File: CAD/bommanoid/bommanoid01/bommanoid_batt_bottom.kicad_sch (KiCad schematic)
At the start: 6 parts

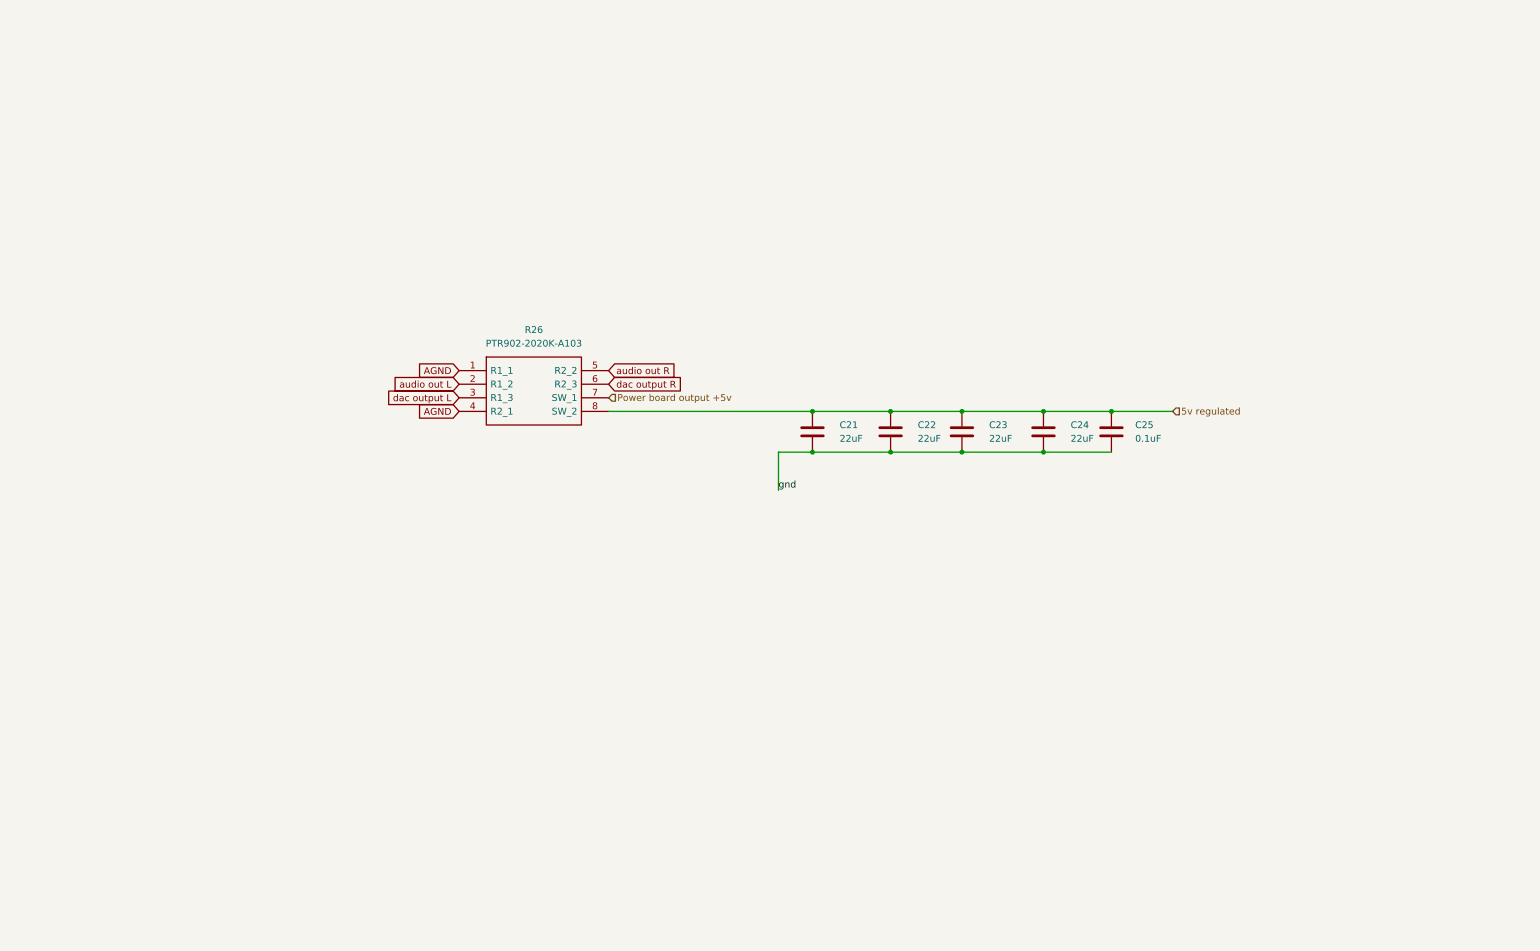
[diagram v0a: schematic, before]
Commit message: progress on bommanoid pcb design adding some winisd simulations
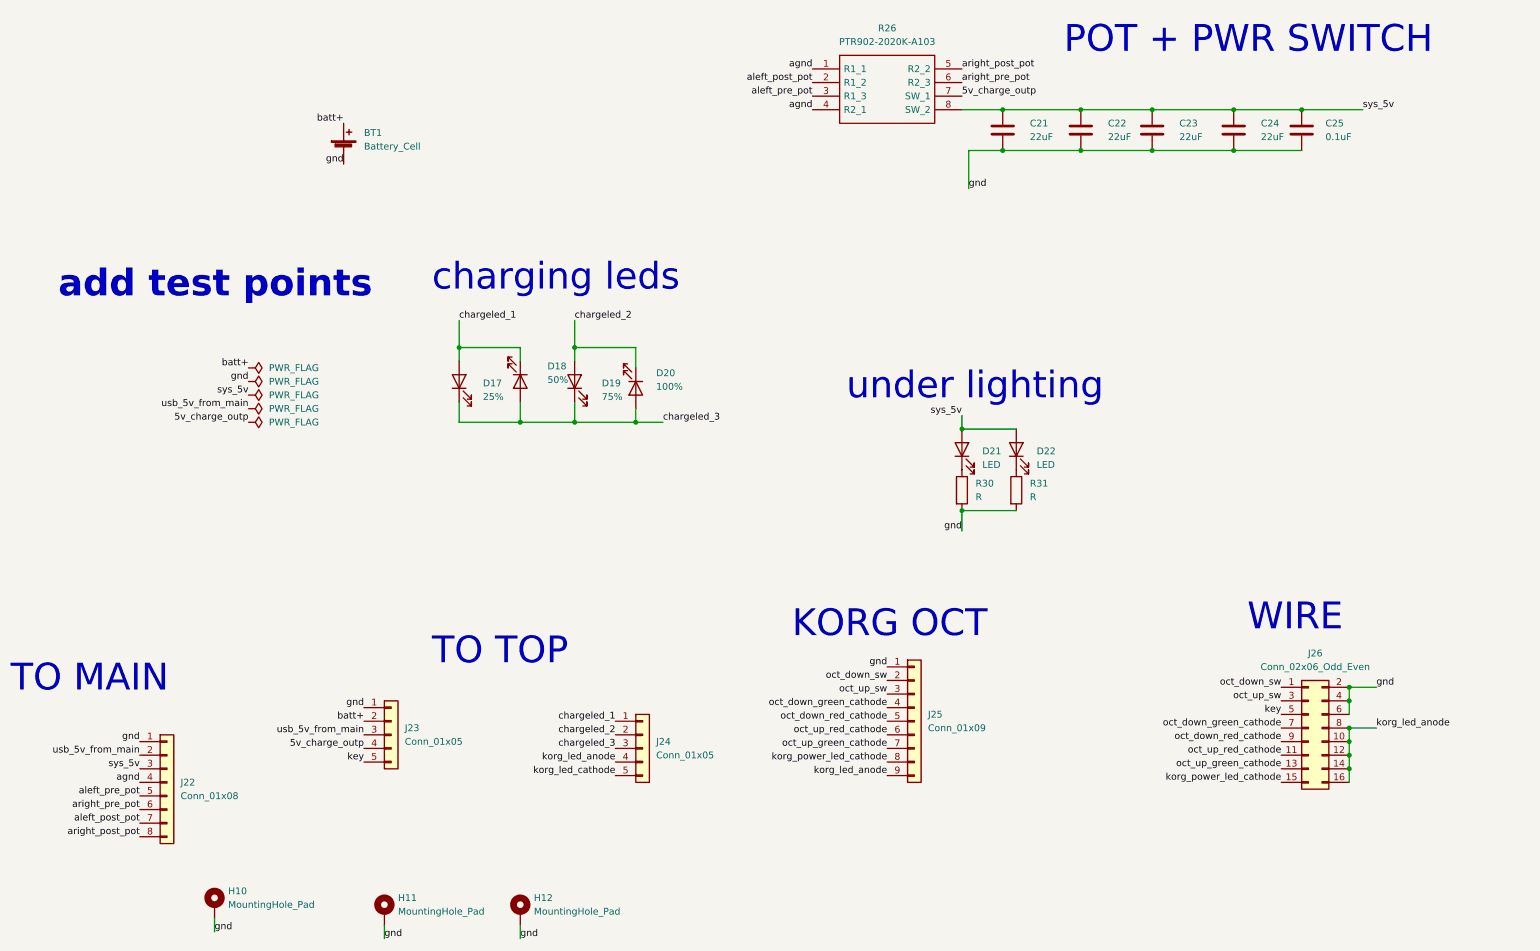
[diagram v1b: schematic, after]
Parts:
- added BT1: Battery_Cell, clarinoid2:KEYSTONE_1043, symbol Device:Battery_Cell
- added D17: 25%, LED_SMD:LED_0805_2012Metric, symbol Device:LED
- added D18: 50%, LED_SMD:LED_0805_2012Metric, symbol Device:LED
- added D19: 75%, LED_SMD:LED_0805_2012Metric, symbol Device:LED
- added D20: 100%, LED_SMD:LED_0805_2012Metric, symbol Device:LED
- added D21, D22: LED, LED_THT:LED_D5.0mm, symbol Device:LED
- added H10, H11, H12: MountingHole_Pad, MountingHole:MountingHole_3.2mm_M3, symbol Mechanical:MountingHole_Pad
- added J22: Conn_01x08, Connector_JST:JST_PH_B8B-PH-K_1x08_P2.00mm_Vertical, symbol Connector_Generic:Conn_01x08
- added J23, J24: Conn_01x05, Connector_PinSocket_2.54mm:PinSocket_1x05_P2.54mm_Vertical, symbol Connector_Generic:Conn_01x05
- added J25: Conn_01x09, Connector_JST:JST_PH_B9B-PH-K_1x09_P2.00mm_Vertical, symbol Connector_Generic:Conn_01x09
- added J26: Conn_02x06_Odd_Even, Connector_PinHeader_2.54mm:PinHeader_2x08_P2.54mm_Vertical, symbol Connector_Generic:Conn_02x08_Odd_Even
- added R30, R31: R, Resistor_THT:R_Axial_DIN0207_L6.3mm_D2.5mm_P10.16mm_Horizontal, symbol Device:R
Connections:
- net gnd: now also BT1.2 (-), H10.1, H11.1, H12.1, J22.1 (Pin_1), J23.1 (Pin_1), J25.1 (Pin_1), J26.2 (Pin_2), J26.4 (Pin_4), J26.6 (Pin_6), R30.2, R31.2
- net 5v regulated renamed sys_5v
- net sys_5v: now also D21.2 (A), D22.2 (A), J22.3 (Pin_3)
- net AGND renamed agnd
- net agnd: now also J22.4 (Pin_4)
- net Power board output +5v renamed 5v_charge_outp
- net 5v_charge_outp: now also J23.4 (Pin_4)
- net audio out L renamed aleft_post_pot
- net aleft_post_pot: now also J22.7 (Pin_7)
- net audio out R renamed aright_post_pot
- net aright_post_pot: now also J22.8 (Pin_8)
- net dac output L renamed aleft_pre_pot
- net aleft_pre_pot: now also J22.5 (Pin_5)
- net dac output R renamed aright_pre_pot
- net aright_pre_pot: now also J22.6 (Pin_6)
- new net: D22.1 (K), R31.1
- new net: D21.1 (K), R30.1
- new net batt+: BT1.1 (+), J23.2 (Pin_2)
- new net chargeled_1: D17.2 (A), D18.1 (K), J24.1 (Pin_1)
- new net chargeled_2: D19.2 (A), D20.1 (K), J24.2 (Pin_2)
- new net chargeled_3: D17.1 (K), D18.2 (A), D19.1 (K), D20.2 (A), J24.3 (Pin_3)
- new net key: J23.5 (Pin_5), J26.5 (Pin_5)
- new net korg_led_anode: J24.4 (Pin_4), J25.9 (Pin_9), J26.10 (Pin_10), J26.12 (Pin_12), J26.14 (Pin_14), J26.16 (Pin_16), J26.8 (Pin_8)
- new net korg_led_cathode: J24.5 (Pin_5)
- new net korg_power_led_cathode: J25.8 (Pin_8), J26.15 (Pin_15)
- new net oct_down_green_cathode: J25.4 (Pin_4), J26.7 (Pin_7)
- new net oct_down_red_cathode: J25.5 (Pin_5), J26.9 (Pin_9)
- new net oct_down_sw: J25.2 (Pin_2), J26.1 (Pin_1)
- new net oct_up_green_cathode: J25.7 (Pin_7), J26.13 (Pin_13)
- new net oct_up_red_cathode: J25.6 (Pin_6), J26.11 (Pin_11)
- new net oct_up_sw: J25.3 (Pin_3), J26.3 (Pin_3)
- new net usb_5v_from_main: J22.2 (Pin_2), J23.3 (Pin_3)
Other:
- note added: "KORG OCT"
- note added: "POT + PWR SWITCH"
- note added: "TO MAIN"
- note added: "TO TOP"
- note added: "WIRE"
- note added: "add test points"
- note added: "charging leds"
- note added: "under lighting"
- moved on the sheet: C21, C22, C23, C24, C25, R26
